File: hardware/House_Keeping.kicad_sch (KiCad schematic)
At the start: 4 parts, among them Q7 SI2302DDS-T1-GE3, U15 CD4051BPWR, U16 CD4051BPWR

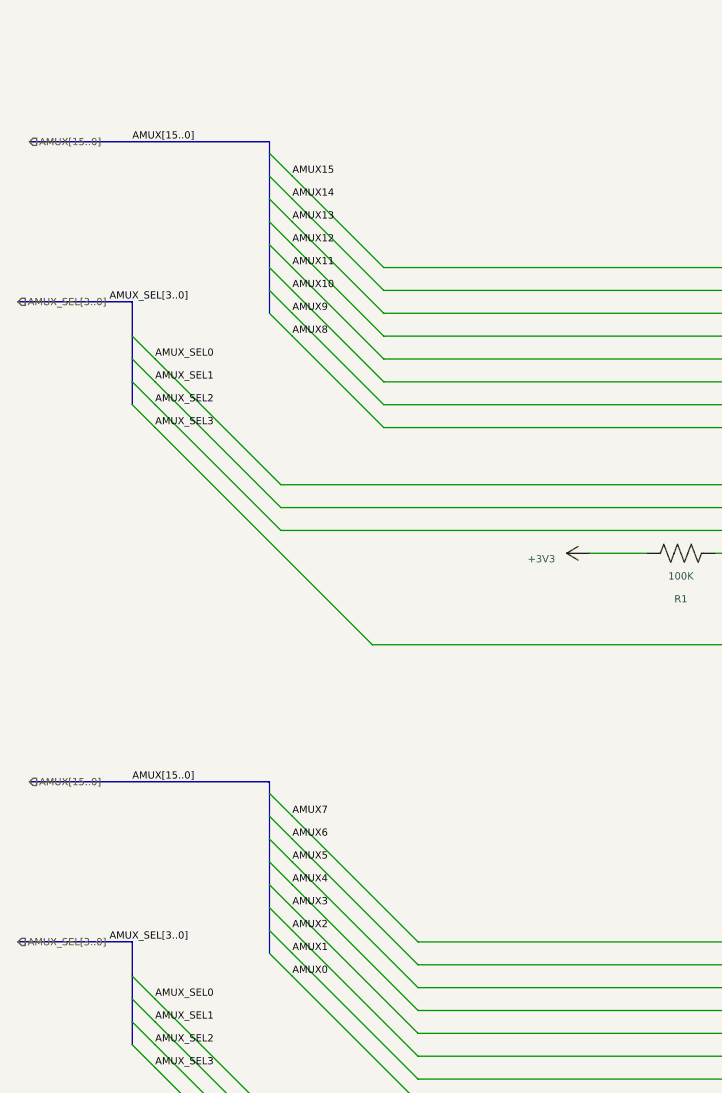
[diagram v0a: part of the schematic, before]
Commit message: hardware: Updating the connectors and connections of the analog signals.
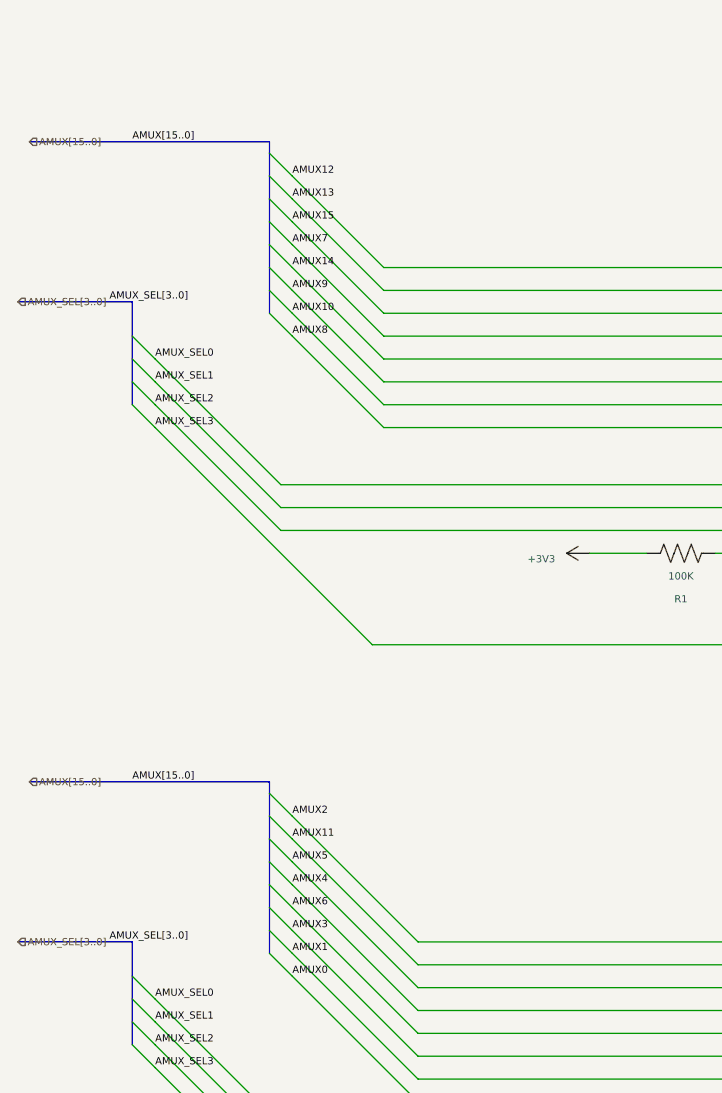
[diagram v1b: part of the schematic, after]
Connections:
- net AMUX10: now also U15.14 (Y1); no longer U15.15 (Y2)
- net AMUX11: now also U16.2 (Y6); no longer U15.12 (Y3)
- net AMUX12: now also U15.4 (Y7); no longer U15.1 (Y4)
- net AMUX13: now also U15.2 (Y6); no longer U15.5 (Y5)
- net AMUX14: now also U15.12 (Y3); no longer U15.2 (Y6)
- net AMUX15: now also U15.5 (Y5); no longer U15.4 (Y7)
- net AMUX2: now also U16.4 (Y7); no longer U16.15 (Y2)
- net AMUX3: now also U16.15 (Y2); no longer U16.12 (Y3)
- net AMUX6: now also U16.12 (Y3); no longer U16.2 (Y6)
- net AMUX7: now also U15.1 (Y4); no longer U16.4 (Y7)
- net AMUX9: now also U15.15 (Y2); no longer U15.14 (Y1)
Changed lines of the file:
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@@
     (effects (font (size 0.8 0.8)) (justify left bottom))
   )
-  (label "AMUX10" (at 60.96 66.04 0) (fields_autoplaced)
+  (label "AMUX10" (at 60.96 68.58 0) (fields_autoplaced)
     (effects (font (size 0.8 0.8)) (justify left bottom))
   )
@@
     (effects (font (size 0.8 0.8)) (justify left bottom))
   )
-  (label "AMUX6" (at 60.96 127 0) (fields_autoplaced)
+  (label "AMUX6" (at 60.96 134.62 0) (fields_autoplaced)
     (effects (font (size 0.8 0.8)) (justify left bottom))
   )
@@
     (effects (font (size 0.8 0.8)) (justify left bottom))
   )
-  (label "AMUX2" (at 60.96 137.16 0) (fields_autoplaced)
+  (label "AMUX2" (at 60.96 124.46 0) (fields_autoplaced)
     (effects (font (size 0.8 0.8)) (justify left bottom))
   )
@@
     (effects (font (size 0.8 0.8)) (justify left bottom))
   )
-  (label "AMUX12" (at 60.96 60.96 0) (fields_autoplaced)
+  (label "AMUX12" (at 60.96 53.34 0) (fields_autoplaced)
     (effects (font (size 0.8 0.8)) (justify left bottom))
   )
@@
     (effects (font (size 0.8 0.8)) (justify left bottom))
   )
-  (label "AMUX11" (at 60.96 63.5 0) (fields_autoplaced)
+  (label "AMUX11" (at 60.96 127 0) (fields_autoplaced)
     (effects (font (size 0.8 0.8)) (justify left bottom))
   )
-  (label "AMUX13" (at 60.96 58.42 0) (fields_autoplaced)
+  (label "AMUX13" (at 60.96 55.88 0) (fields_autoplaced)
     (effects (font (size 0.8 0.8)) (justify left bottom))
   )
@@
     (effects (font (size 0.8 0.8)) (justify left bottom))
   )
-  (label "AMUX15" (at 60.96 53.34 0) (fields_autoplaced)
+  (label "AMUX15" (at 60.96 58.42 0) (fields_autoplaced)
     (effects (font (size 0.8 0.8)) (justify left bottom))
   )
@@
     (effects (font (size 0.8 0.8)) (justify left bottom))
   )
-  (label "AMUX9" (at 60.96 68.58 0) (fields_autoplaced)
+  (label "AMUX9" (at 60.96 66.04 0) (fields_autoplaced)
     (effects (font (size 0.8 0.8)) (justify left bottom))
   )
-  (label "AMUX3" (at 60.96 134.62 0) (fields_autoplaced)
+  (label "AMUX3" (at 60.96 137.16 0) (fields_autoplaced)
     (effects (font (size 0.8 0.8)) (justify left bottom))
   )
-  (label "AMUX14" (at 60.96 55.88 0) (fields_autoplaced)
+  (label "AMUX14" (at 60.96 63.5 0) (fields_autoplaced)
     (effects (font (size 0.8 0.8)) (justify left bottom))
   )
@@
     (effects (font (size 0.8 0.8)) (justify left bottom))
   )
-  (label "AMUX7" (at 60.96 124.46 0) (fields_autoplaced)
+  (label "AMUX7" (at 60.96 60.96 0) (fields_autoplaced)
     (effects (font (size 0.8 0.8)) (justify left bottom))
   )

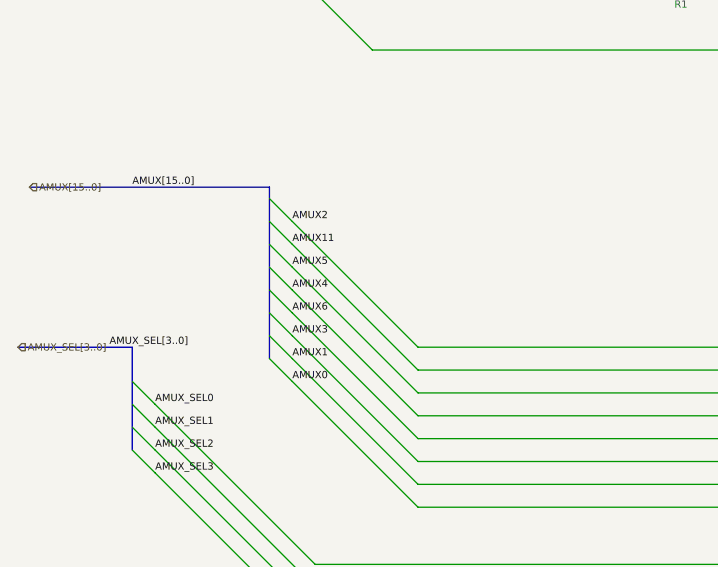
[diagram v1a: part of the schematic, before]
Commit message: hardware: House Keeping and Energy Distribution circuit routing
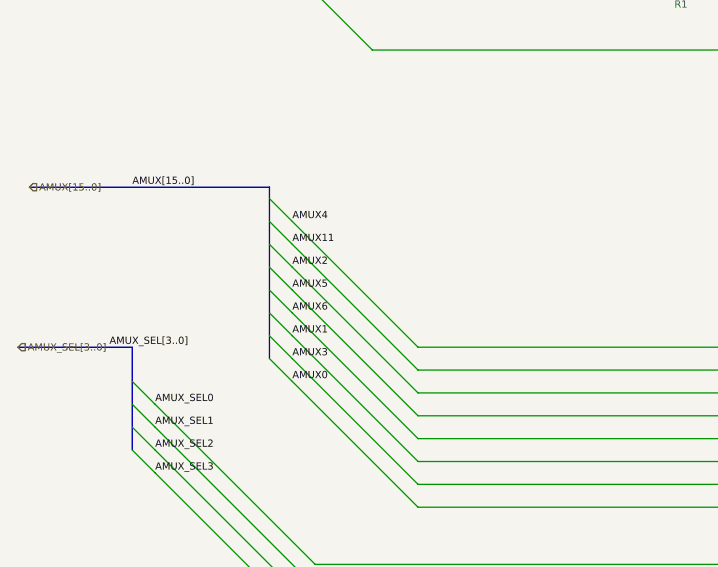
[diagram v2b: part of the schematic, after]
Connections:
- net AMUX1: now also U16.15 (Y2); no longer U16.14 (Y1)
- net AMUX2: now also U16.5 (Y5); no longer U16.4 (Y7)
- net AMUX3: now also U16.14 (Y1); no longer U16.15 (Y2)
- net AMUX4: now also U16.4 (Y7); no longer U16.1 (Y4)
- net AMUX5: now also U16.1 (Y4); no longer U16.5 (Y5)
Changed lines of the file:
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@@
     (effects (font (size 0.8 0.8)) (justify left bottom))
   )
-  (label "AMUX5" (at 60.96 129.54 0) (fields_autoplaced)
+  (label "AMUX5" (at 60.96 132.08 0) (fields_autoplaced)
     (effects (font (size 0.8 0.8)) (justify left bottom))
   )
-  (label "AMUX4" (at 60.96 132.08 0) (fields_autoplaced)
-    (effects (font (size 0.8 0.8)) (justify left bottom))
-  )
-  (label "AMUX1" (at 60.96 139.7 0) (fields_autoplaced)
+  (label "AMUX1" (at 60.96 137.16 0) (fields_autoplaced)
     (effects (font (size 0.8 0.8)) (justify left bottom))
   )
@@
     (effects (font (size 0.8 0.8)) (justify left bottom))
   )
-  (label "AMUX2" (at 60.96 124.46 0) (fields_autoplaced)
+  (label "AMUX2" (at 60.96 129.54 0) (fields_autoplaced)
     (effects (font (size 0.8 0.8)) (justify left bottom))
   )
@@
   )
   (label "AMUX_SEL3" (at 45.72 152.4 0) (fields_autoplaced)
+    (effects (font (size 0.8 0.8)) (justify left bottom))
+  )
+  (label "AMUX4" (at 60.96 124.46 0) (fields_autoplaced)
     (effects (font (size 0.8 0.8)) (justify left bottom))
   )
@@
     (effects (font (size 0.8 0.8)) (justify left bottom))
   )
-  (label "AMUX3" (at 60.96 137.16 0) (fields_autoplaced)
+  (label "AMUX3" (at 60.96 139.7 0) (fields_autoplaced)
     (effects (font (size 0.8 0.8)) (justify left bottom))
   )

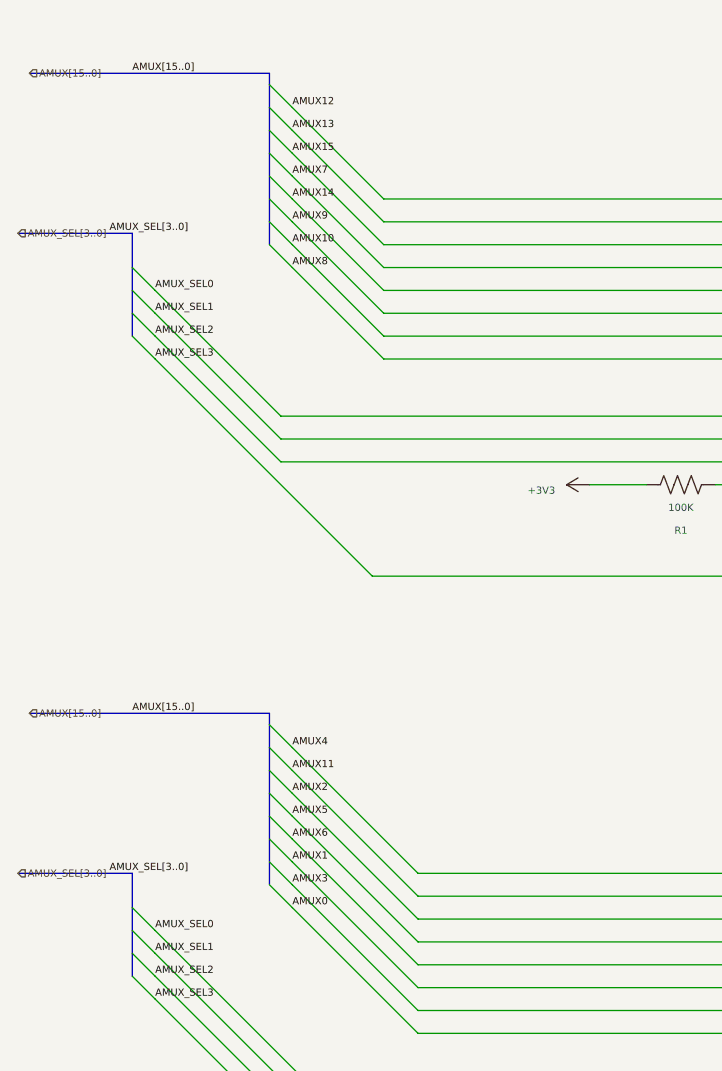
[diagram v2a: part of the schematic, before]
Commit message: hardware: First version of the RE2PS layout with all components connected.
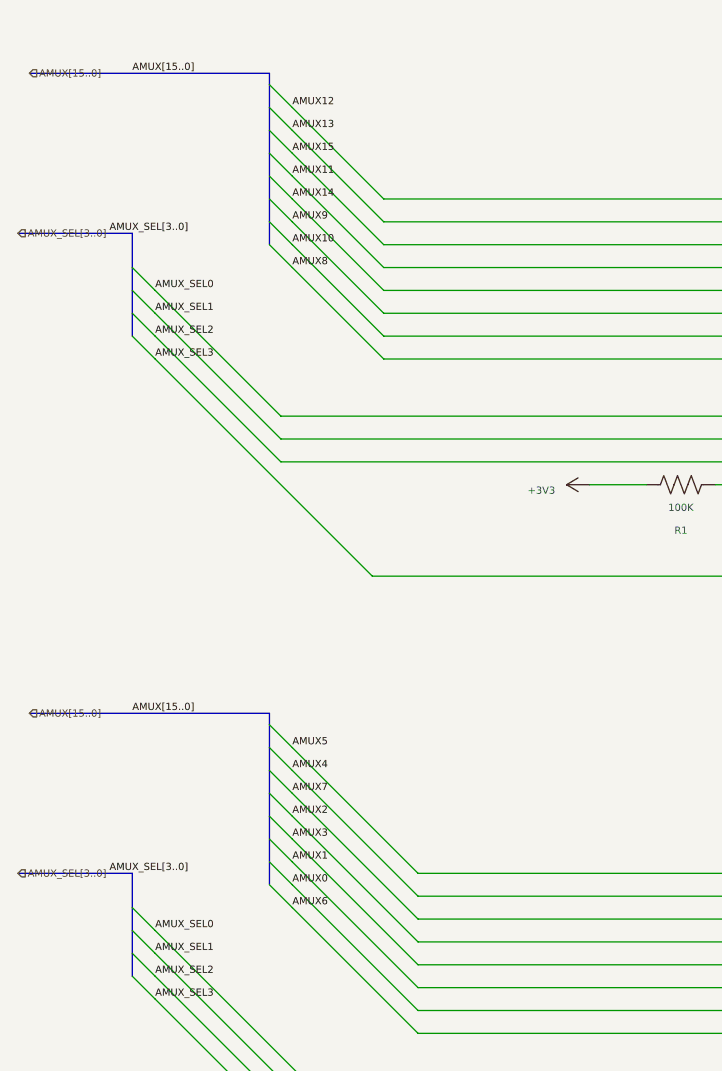
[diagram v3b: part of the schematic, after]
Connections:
- net AMUX0: now also U16.14 (Y1); no longer U16.13 (Y0)
- net AMUX11: now also U15.1 (Y4); no longer U16.2 (Y6)
- net AMUX2: now also U16.1 (Y4); no longer U16.5 (Y5)
- net AMUX3: now also U16.12 (Y3); no longer U16.14 (Y1)
- net AMUX4: now also U16.2 (Y6); no longer U16.4 (Y7)
- net AMUX5: now also U16.4 (Y7); no longer U16.1 (Y4)
- net AMUX6: now also U16.13 (Y0); no longer U16.12 (Y3)
- net AMUX7: now also U16.5 (Y5); no longer U15.1 (Y4)
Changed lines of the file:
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@@
     (effects (font (size 0.8 0.8)) (justify left bottom))
   )
-  (label "AMUX5" (at 60.96 132.08 0) (fields_autoplaced)
+  (label "AMUX5" (at 60.96 124.46 0) (fields_autoplaced)
     (effects (font (size 0.8 0.8)) (justify left bottom))
   )
@@
     (effects (font (size 0.8 0.8)) (justify left bottom))
   )
-  (label "AMUX6" (at 60.96 134.62 0) (fields_autoplaced)
+  (label "AMUX6" (at 60.96 142.24 0) (fields_autoplaced)
     (effects (font (size 0.8 0.8)) (justify left bottom))
   )
@@
     (effects (font (size 0.8 0.8)) (justify left bottom))
   )
-  (label "AMUX2" (at 60.96 129.54 0) (fields_autoplaced)
+  (label "AMUX2" (at 60.96 132.08 0) (fields_autoplaced)
     (effects (font (size 0.8 0.8)) (justify left bottom))
   )
@@
     (effects (font (size 0.8 0.8)) (justify left bottom))
   )
-  (label "AMUX11" (at 60.96 127 0) (fields_autoplaced)
+  (label "AMUX11" (at 60.96 60.96 0) (fields_autoplaced)
     (effects (font (size 0.8 0.8)) (justify left bottom))
   )
@@
     (effects (font (size 0.8 0.8)) (justify left bottom))
   )
-  (label "AMUX4" (at 60.96 124.46 0) (fields_autoplaced)
+  (label "AMUX4" (at 60.96 127 0) (fields_autoplaced)
     (effects (font (size 0.8 0.8)) (justify left bottom))
   )
@@
     (effects (font (size 0.8 0.8)) (justify left bottom))
   )
-  (label "AMUX0" (at 60.96 142.24 0) (fields_autoplaced)
+  (label "AMUX0" (at 60.96 139.7 0) (fields_autoplaced)
     (effects (font (size 0.8 0.8)) (justify left bottom))
   )
@@
     (effects (font (size 0.8 0.8)) (justify left bottom))
   )
-  (label "AMUX3" (at 60.96 139.7 0) (fields_autoplaced)
+  (label "AMUX3" (at 60.96 134.62 0) (fields_autoplaced)
     (effects (font (size 0.8 0.8)) (justify left bottom))
   )
@@
     (effects (font (size 0.8 0.8)) (justify left bottom))
   )
-  (label "AMUX7" (at 60.96 60.96 0) (fields_autoplaced)
+  (label "AMUX7" (at 60.96 129.54 0) (fields_autoplaced)
     (effects (font (size 0.8 0.8)) (justify left bottom))
   )

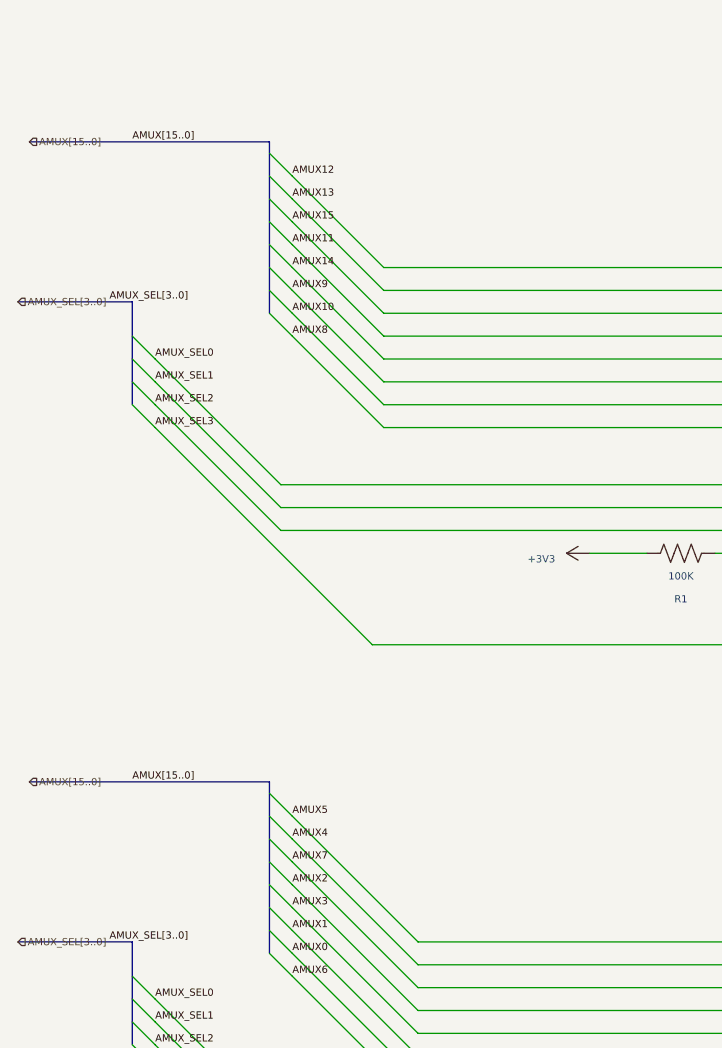
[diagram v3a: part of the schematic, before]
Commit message: hardware: Minor modifications and changing the position of some circuits.
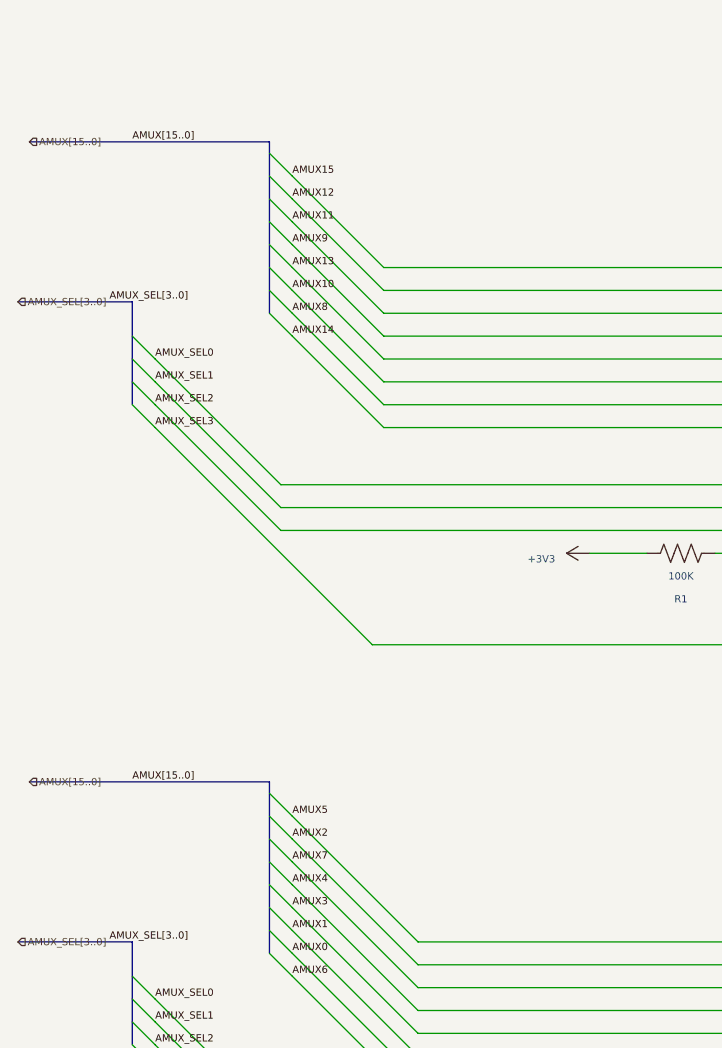
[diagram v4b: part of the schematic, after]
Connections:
- net AMUX10: now also U15.15 (Y2); no longer U15.14 (Y1)
- net AMUX11: now also U15.5 (Y5); no longer U15.1 (Y4)
- net AMUX12: now also U15.2 (Y6); no longer U15.4 (Y7)
- net AMUX13: now also U15.12 (Y3); no longer U15.2 (Y6)
- net AMUX14: now also U15.13 (Y0); no longer U15.12 (Y3)
- net AMUX15: now also U15.4 (Y7); no longer U15.5 (Y5)
- net AMUX2: now also U16.2 (Y6); no longer U16.1 (Y4)
- net AMUX4: now also U16.1 (Y4); no longer U16.2 (Y6)
- net AMUX8: now also U15.14 (Y1); no longer U15.13 (Y0)
- net AMUX9: now also U15.1 (Y4); no longer U15.15 (Y2)
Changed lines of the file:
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@@
     (effects (font (size 0.8 0.8)) (justify left bottom))
   )
-  (label "AMUX10" (at 60.96 68.58 0) (fields_autoplaced)
+  (label "AMUX10" (at 60.96 66.04 0) (fields_autoplaced)
     (effects (font (size 0.8 0.8)) (justify left bottom))
   )
@@
     (effects (font (size 0.8 0.8)) (justify left bottom))
   )
-  (label "AMUX2" (at 60.96 132.08 0) (fields_autoplaced)
+  (label "AMUX2" (at 60.96 127 0) (fields_autoplaced)
     (effects (font (size 0.8 0.8)) (justify left bottom))
   )
@@
     (effects (font (size 0.8 0.8)) (justify left bottom))
   )
-  (label "AMUX12" (at 60.96 53.34 0) (fields_autoplaced)
+  (label "AMUX12" (at 60.96 55.88 0) (fields_autoplaced)
     (effects (font (size 0.8 0.8)) (justify left bottom))
   )
@@
     (effects (font (size 0.8 0.8)) (justify left bottom))
   )
-  (label "AMUX11" (at 60.96 60.96 0) (fields_autoplaced)
+  (label "AMUX11" (at 60.96 58.42 0) (fields_autoplaced)
     (effects (font (size 0.8 0.8)) (justify left bottom))
   )
-  (label "AMUX13" (at 60.96 55.88 0) (fields_autoplaced)
+  (label "AMUX13" (at 60.96 63.5 0) (fields_autoplaced)
     (effects (font (size 0.8 0.8)) (justify left bottom))
   )
@@
     (effects (font (size 0.8 0.8)) (justify left bottom))
   )
-  (label "AMUX4" (at 60.96 127 0) (fields_autoplaced)
+  (label "AMUX4" (at 60.96 132.08 0) (fields_autoplaced)
     (effects (font (size 0.8 0.8)) (justify left bottom))
   )
-  (label "AMUX15" (at 60.96 58.42 0) (fields_autoplaced)
+  (label "AMUX15" (at 60.96 53.34 0) (fields_autoplaced)
     (effects (font (size 0.8 0.8)) (justify left bottom))
   )
@@
     (effects (font (size 0.8 0.8)) (justify left bottom))
   )
-  (label "AMUX8" (at 60.96 71.12 0) (fields_autoplaced)
+  (label "AMUX8" (at 60.96 68.58 0) (fields_autoplaced)
     (effects (font (size 0.8 0.8)) (justify left bottom))
   )
@@
     (effects (font (size 0.8 0.8)) (justify left bottom))
   )
-  (label "AMUX9" (at 60.96 66.04 0) (fields_autoplaced)
+  (label "AMUX9" (at 60.96 60.96 0) (fields_autoplaced)
     (effects (font (size 0.8 0.8)) (justify left bottom))
   )
@@
     (effects (font (size 0.8 0.8)) (justify left bottom))
   )
-  (label "AMUX14" (at 60.96 63.5 0) (fields_autoplaced)
+  (label "AMUX14" (at 60.96 71.12 0) (fields_autoplaced)
     (effects (font (size 0.8 0.8)) (justify left bottom))
   )
